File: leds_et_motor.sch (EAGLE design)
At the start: 4 parts, among them IC1 74LS595N, IC2 74LS595N

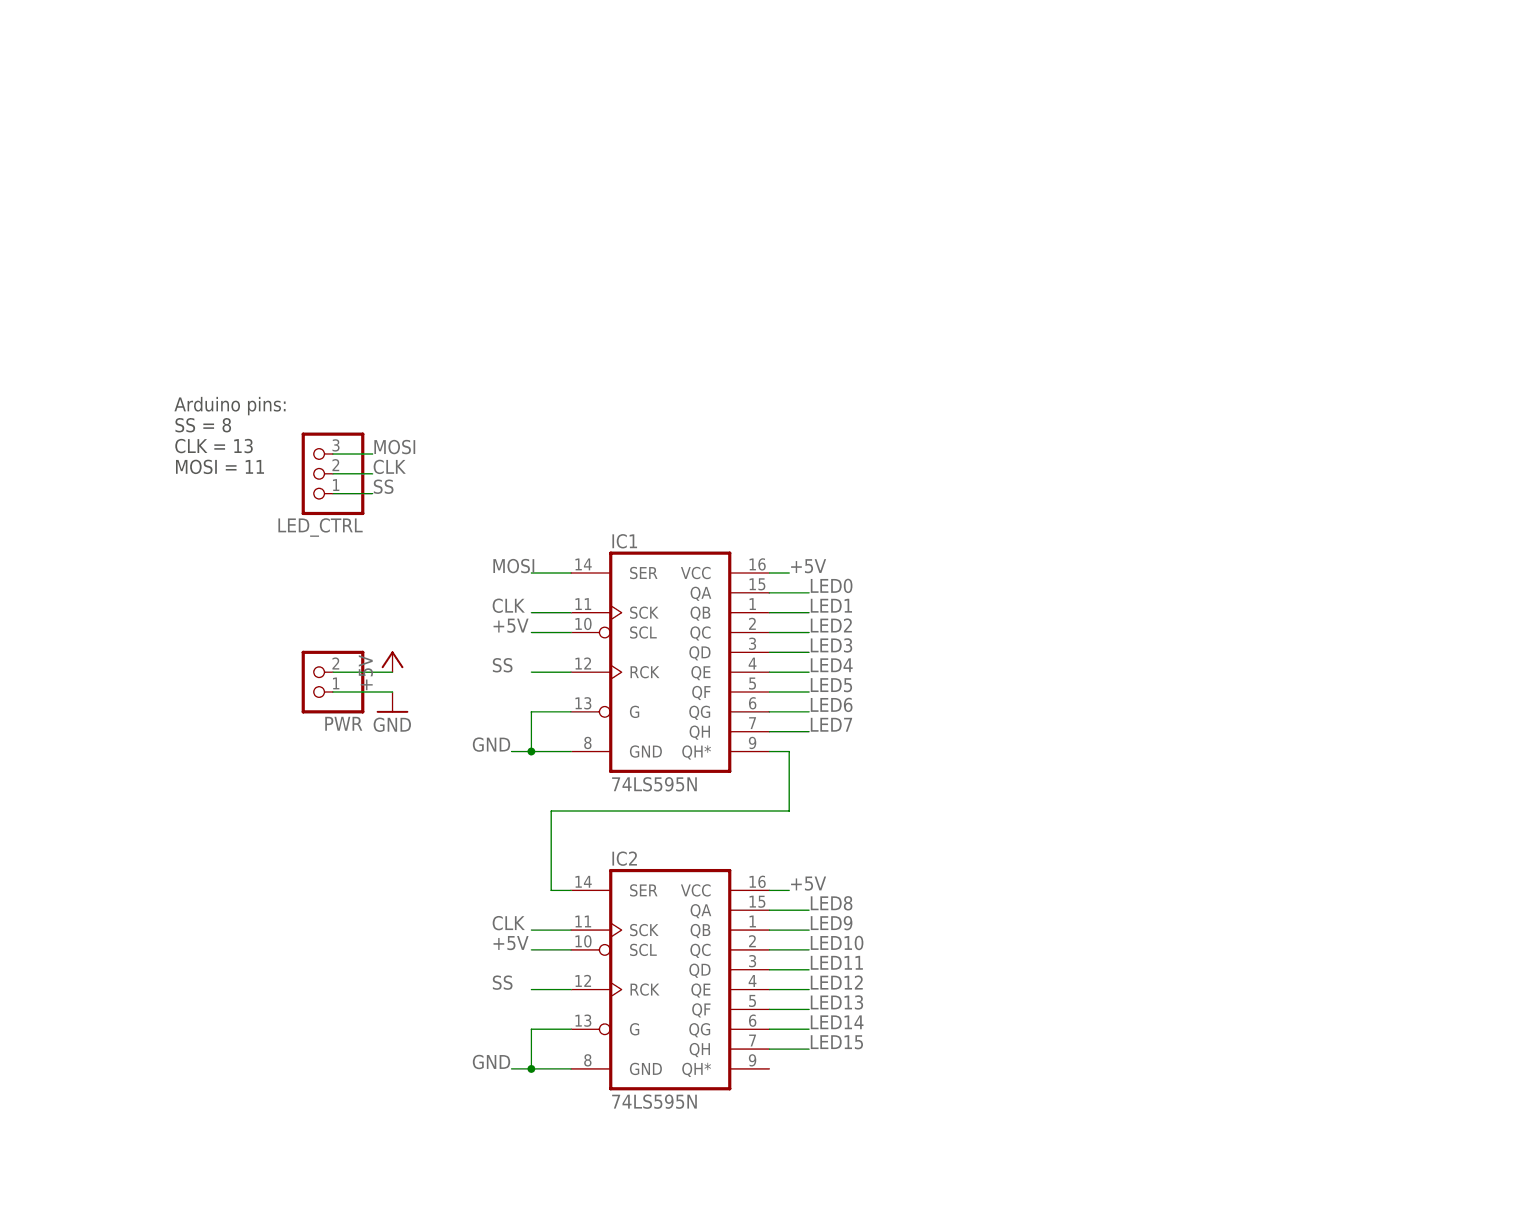
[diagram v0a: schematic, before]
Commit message: added the darlington and pin-headers for outputs
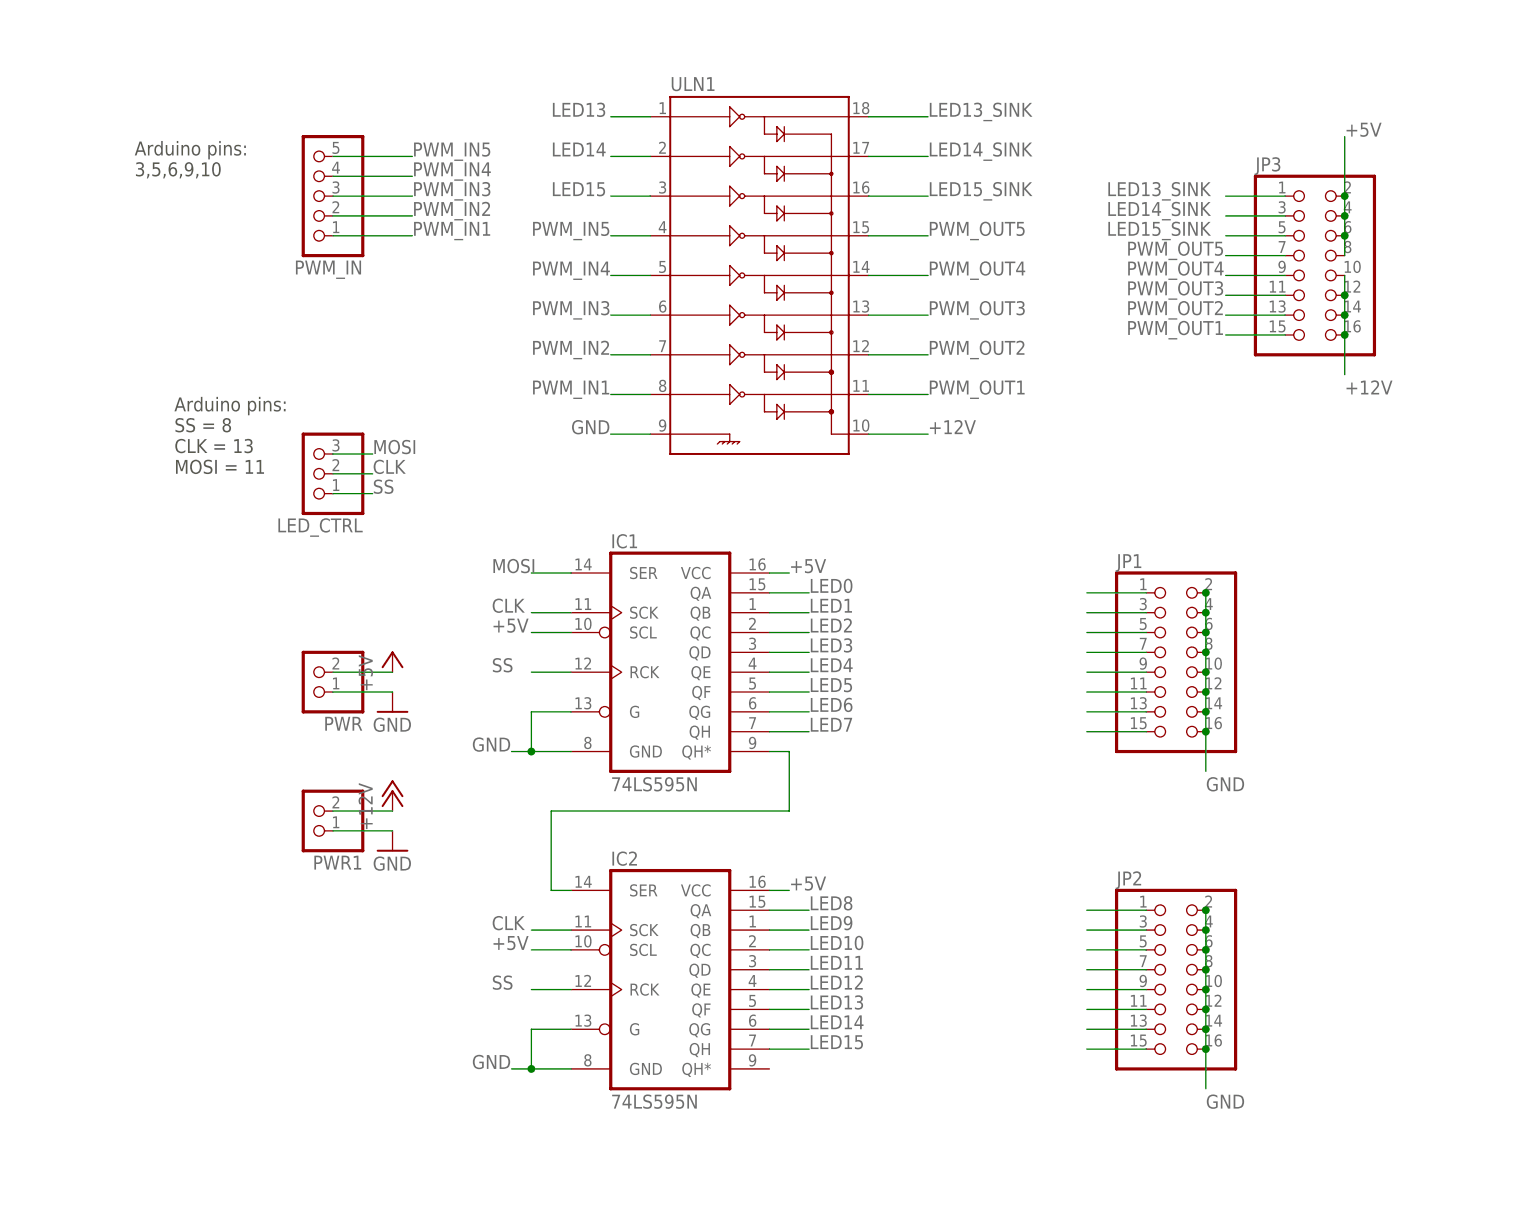
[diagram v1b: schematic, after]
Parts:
- added JP1, JP2, JP3: (no value), pinhead:PINHD-2X8/90
- added PWM_IN: (no value), pinhead:PINHD-1X5
- added PWR1: (no value), pinhead:PINHD-1X2
- added ULN1: (no value), SparkFun-PowerIC:ULN2803DIP
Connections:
- new net +12V: JP3.10, JP3.12, JP3.14, JP3.16, PWR1.2, ULN1.10
- new net LED13_SINK: JP3.1, ULN1.18
- new net LED14_SINK: JP3.3, ULN1.17
- new net LED15_SINK: JP3.5, ULN1.16
- new net N$30: JP1.1
- new net N$31: JP1.3
- new net N$32: JP1.5
- new net N$33: JP1.7
- new net N$34: JP1.9
- new net N$35: JP1.11
- new net N$36: JP1.13
- new net N$37: JP1.15
- new net N$38: JP2.1
- new net N$39: JP2.3
- new net N$40: JP2.5
- new net N$41: JP2.7
- new net N$42: JP2.9
- new net N$43: JP2.11
- new net N$44: JP2.13
- new net N$45: JP2.15
- new net PWM_IN1: PWM_IN.1, ULN1.8
- new net PWM_IN2: PWM_IN.2, ULN1.7
- new net PWM_IN3: PWM_IN.3, ULN1.6
- new net PWM_IN4: PWM_IN.4, ULN1.5
- new net PWM_IN5: PWM_IN.5, ULN1.4
- new net PWM_OUT1: JP3.15, ULN1.11
- new net PWM_OUT2: JP3.13, ULN1.12
- new net PWM_OUT3: JP3.11, ULN1.13
- new net PWM_OUT4: JP3.9, ULN1.14
- new net PWM_OUT5: JP3.7, ULN1.15
- net +5V: now also JP3.2, JP3.4, JP3.6, JP3.8
- net GND: now also JP1.10, JP1.12, JP1.14, JP1.16, JP1.2, JP1.4, JP1.6, JP1.8, JP2.10, JP2.12, JP2.14, JP2.16, JP2.2, JP2.4, JP2.6, JP2.8, PWR1.1, ULN1.9
- net LED13: now also ULN1.1
- net LED14: now also ULN1.2
- net LED15: now also ULN1.3
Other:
- note added: "Arduino pins: 3,5,6,9,10"

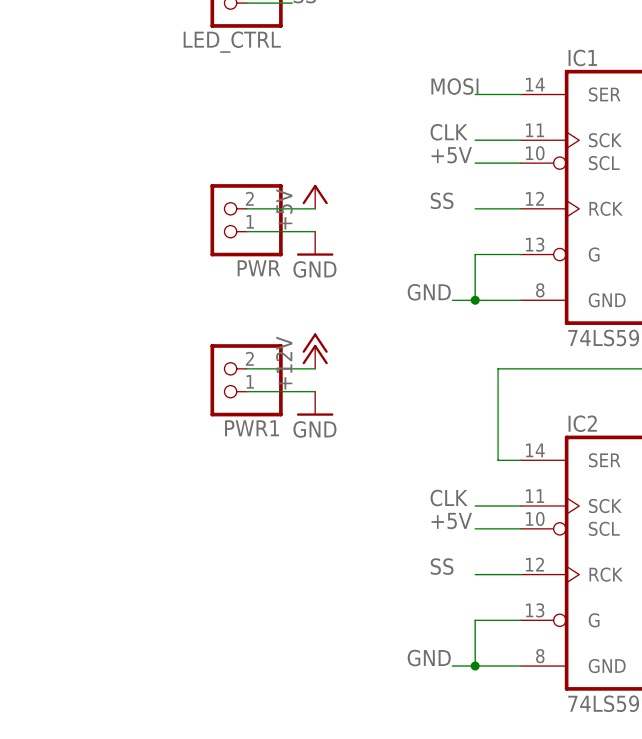
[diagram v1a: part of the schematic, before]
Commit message: bring 12V in trhough this board, use 4 wires to pass the 12V to the arduino and 5V back
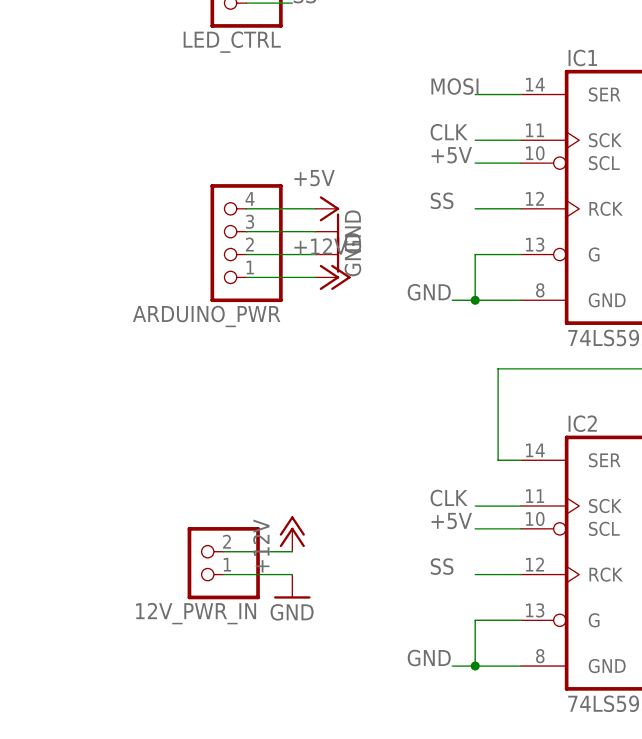
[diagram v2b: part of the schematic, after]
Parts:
- removed PWR, PWR1: (no value), pinhead:PINHD-1X2
- added 12V_PWR_IN: (no value), pinhead:PINHD-1X2
- added ARDUINO_PWR: (no value), pinhead:PINHD-1X4
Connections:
- net +12V: now also 12V_PWR_IN.2, ARDUINO_PWR.1; no longer PWR1.2
- net +5V: now also ARDUINO_PWR.4; no longer PWR.2
- net GND: now also 12V_PWR_IN.1, ARDUINO_PWR.2, ARDUINO_PWR.3; no longer PWR.1, PWR1.1
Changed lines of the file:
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@@
 <part name="LED_CTRL" library="pinhead" deviceset="PINHD-1X3" device=""/>
 <part name="IC1" library="SparkFun-DigitalIC" deviceset="74*595" device="N" technology="LS"/>
-<part name="PWR" library="pinhead" deviceset="PINHD-1X2" device=""/>
 <part name="GND1" library="supply1" deviceset="GND" device=""/>
 <part name="P+1" library="supply1" deviceset="+5V" device=""/>
 <part name="IC2" library="SparkFun-DigitalIC" deviceset="74*595" device="N" technology="LS"/>
 <part name="ULN1" library="SparkFun-PowerIC" deviceset="ULN2803" device="DIP"/>
-<part name="PWR1" library="pinhead" deviceset="PINHD-1X2" device=""/>
 <part name="GND2" library="supply1" deviceset="GND" device=""/>
 <part name="P+2" library="supply1" deviceset="+12V" device=""/>
@@
 <part name="JP1" library="pinhead" deviceset="PINHD-2X8" device="/90"/>
 <part name="JP2" library="pinhead" deviceset="PINHD-2X8" device="/90"/>
+<part name="12V_PWR_IN" library="pinhead" deviceset="PINHD-1X2" device=""/>
+<part name="GND3" library="supply1" deviceset="GND" device=""/>
+<part name="P+3" library="supply1" deviceset="+12V" device=""/>
+<part name="ARDUINO_PWR" library="pinhead" deviceset="PINHD-1X4" device=""/>
 </parts>
 <sheets>
@@
 <instance part="LED_CTRL" gate="A" x="7.62" y="66.04" rot="R180"/>
 <instance part="IC1" gate="A" x="50.8" y="43.18"/>
-<instance part="PWR" gate="G$1" x="7.62" y="40.64" rot="R180"/>
-<instance part="GND1" gate="1" x="17.78" y="35.56"/>
-<instance part="P+1" gate="1" x="17.78" y="43.18"/>
+<instance part="GND1" gate="1" x="20.32" y="38.1" rot="R90"/>
+<instance part="P+1" gate="1" x="20.32" y="40.64" rot="R270"/>
 <instance part="IC2" gate="A" x="50.8" y="2.54"/>
 <instance part="ULN1" gate="G$1" x="63.5" y="93.98"/>
-<instance part="PWR1" gate="G$1" x="7.62" y="22.86" rot="R180"/>
-<instance part="GND2" gate="1" x="17.78" y="17.78"/>
-<instance part="P+2" gate="1" x="17.78" y="25.4"/>
+<instance part="GND2" gate="1" x="20.32" y="35.56" rot="R90"/>
+<instance part="P+2" gate="1" x="20.32" y="33.02" rot="R270"/>
 <instance part="PWM_IN" gate="A" x="7.62" y="101.6" rot="R180"/>
 <instance part="JP3" gate="A" x="134.62" y="93.98"/>
 <instance part="JP1" gate="A" x="116.84" y="43.18"/>
 <instance part="JP2" gate="A" x="116.84" y="2.54"/>
+<instance part="12V_PWR_IN" gate="G$1" x="5.08" y="2.54" rot="R180"/>
+<instance part="GND3" gate="1" x="15.24" y="-2.54"/>
+<instance part="P+3" gate="1" x="15.24" y="5.08"/>
+<instance part="ARDUINO_PWR" gate="A" x="7.62" y="38.1" rot="R180"/>
 </instances>
 <busses>
@@
 <net name="GND" class="0">
 <segment>
-<pinref part="PWR" gate="G$1" pin="1"/>
 <wire x1="10.16" y1="38.1" x2="17.78" y2="38.1" width="0.1524" layer="91"/>
 <pinref part="GND1" gate="1" pin="GND"/>
+<pinref part="ARDUINO_PWR" gate="A" pin="3"/>
 </segment>
 <segment>
@@
 </segment>
 <segment>
-<pinref part="PWR1" gate="G$1" pin="1"/>
-<wire x1="10.16" y1="20.32" x2="17.78" y2="20.32" width="0.1524" layer="91"/>
+<wire x1="10.16" y1="35.56" x2="17.78" y2="35.56" width="0.1524" layer="91"/>
 <pinref part="GND2" gate="1" pin="GND"/>
+<pinref part="ARDUINO_PWR" gate="A" pin="2"/>
 </segment>
 <segment>
@@
 <label x="121.92" y="-15.24" size="1.778" layer="95"/>
 </segment>
+<segment>
+<pinref part="12V_PWR_IN" gate="G$1" pin="1"/>
+<wire x1="7.62" y1="0" x2="15.24" y2="0" width="0.1524" layer="91"/>
+<pinref part="GND3" gate="1" pin="GND"/>
+</segment>
 </net>
 <net name="+5V" class="0">
 <segment>
-<pinref part="PWR" gate="G$1" pin="2"/>
 <wire x1="10.16" y1="40.64" x2="17.78" y2="40.64" width="0.1524" layer="91"/>
 <pinref part="P+1" gate="1" pin="+5V"/>
+<pinref part="ARDUINO_PWR" gate="A" pin="4"/>
 </segment>
 <segment>
@@
 <net name="+12V" class="0">
 <segment>
-<pinref part="PWR1" gate="G$1" pin="2"/>
-<wire x1="10.16" y1="22.86" x2="17.78" y2="22.86" width="0.1524" layer="91"/>
+<wire x1="10.16" y1="33.02" x2="17.78" y2="33.02" width="0.1524" layer="91"/>
 <pinref part="P+2" gate="1" pin="+12V"/>
+<pinref part="ARDUINO_PWR" gate="A" pin="1"/>
 </segment>
 <segment>
@@
 <label x="139.7" y="76.2" size="1.778" layer="95"/>
 </segment>
-</net>
+<segment>
+<pinref part="12V_PWR_IN" gate="G$1" pin="2"/>
+<wire x1="7.62" y1="2.54" x2="15.24" y2="2.54" width="0.1524" layer="91"/>
+<pinref part="P+3" gate="1" pin="+12V"/>
+</segment>
+</net>

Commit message: these got switched around
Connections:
- net CLK: now also LED_CTRL.1; no longer LED_CTRL.2
- net SS: now also LED_CTRL.2; no longer LED_CTRL.1
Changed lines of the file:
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@@
-</segment>
-<segment>
-<pinref part="LED_CTRL" gate="A" pin="2"/>
-<wire x1="10.16" y1="66.04" x2="15.24" y2="66.04" width="0.1524" layer="91"/>
-<label x="15.24" y="66.04" size="1.778" layer="95"/>
 </segment>
 <segment>
@@
 <wire x1="40.64" y1="7.62" x2="35.56" y2="7.62" width="0.1524" layer="91"/>
 <label x="30.48" y="7.62" size="1.778" layer="95"/>
+</segment>
+<segment>
+<pinref part="LED_CTRL" gate="A" pin="1"/>
+<wire x1="10.16" y1="63.5" x2="15.24" y2="63.5" width="0.1524" layer="91"/>
+<label x="15.24" y="63.5" size="1.778" layer="95"/>
 </segment>
 </net>
@@
 </segment>
 <segment>
-<pinref part="LED_CTRL" gate="A" pin="1"/>
-<wire x1="10.16" y1="63.5" x2="15.24" y2="63.5" width="0.1524" layer="91"/>
-<label x="15.24" y="63.5" size="1.778" layer="95"/>
-</segment>
-<segment>
 <pinref part="IC2" gate="A" pin="RCK"/>
 <wire x1="40.64" y1="0" x2="35.56" y2="0" width="0.1524" layer="91"/>
 <label x="30.48" y="0" size="1.778" layer="95"/>
 </segment>
+<segment>
+<pinref part="LED_CTRL" gate="A" pin="2"/>
+<wire x1="10.16" y1="66.04" x2="15.24" y2="66.04" width="0.1524" layer="91"/>
+<label x="15.24" y="66.04" size="1.778" layer="95"/>
+</segment>
 </net>

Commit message: reminders
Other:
- note added: "TODO: LED13-15 signals are not wired to the darlington right now, will maybe do it later if it's needed."
- note added: "TODO: mark the QA output to correct pin (forgot to shift the 595s by one...)"
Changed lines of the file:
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@@
 <text x="-15.24" y="104.14" size="1.778" layer="97">Arduino pins:
 3,5,6,9,10</text>
+<text x="78.74" y="17.78" size="1.778" layer="97">TODO: mark the QA output to correct pin
+(forgot to shift the 595s by one...) </text>
+<text x="25.4" y="119.38" size="1.778" layer="97">TODO: LED13-15 signals are not wired to the darlington
+right now, will maybe do it later if it's needed.</text>
 </plain>
 <instances>
